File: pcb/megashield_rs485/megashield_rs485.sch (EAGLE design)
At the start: 16 parts, among them J11 DYNAMIXEL_RS485, U1 SN75176B

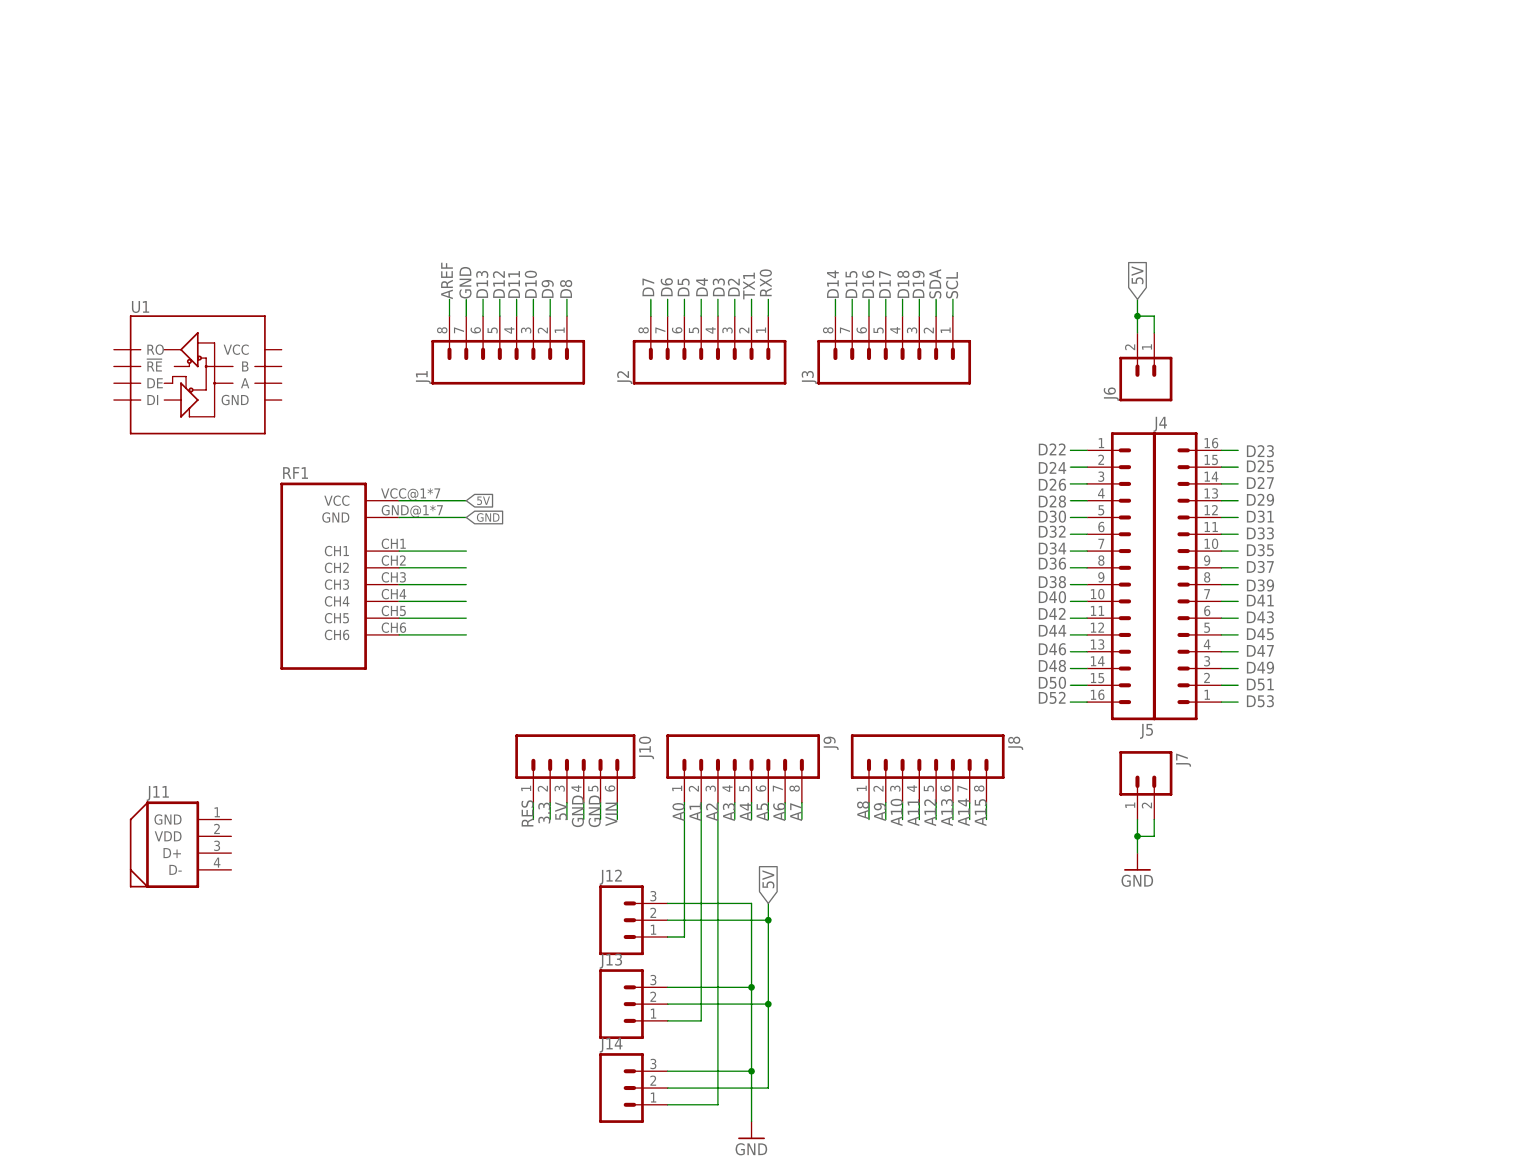
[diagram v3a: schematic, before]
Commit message: PCB con elementos para conexion de pantalla
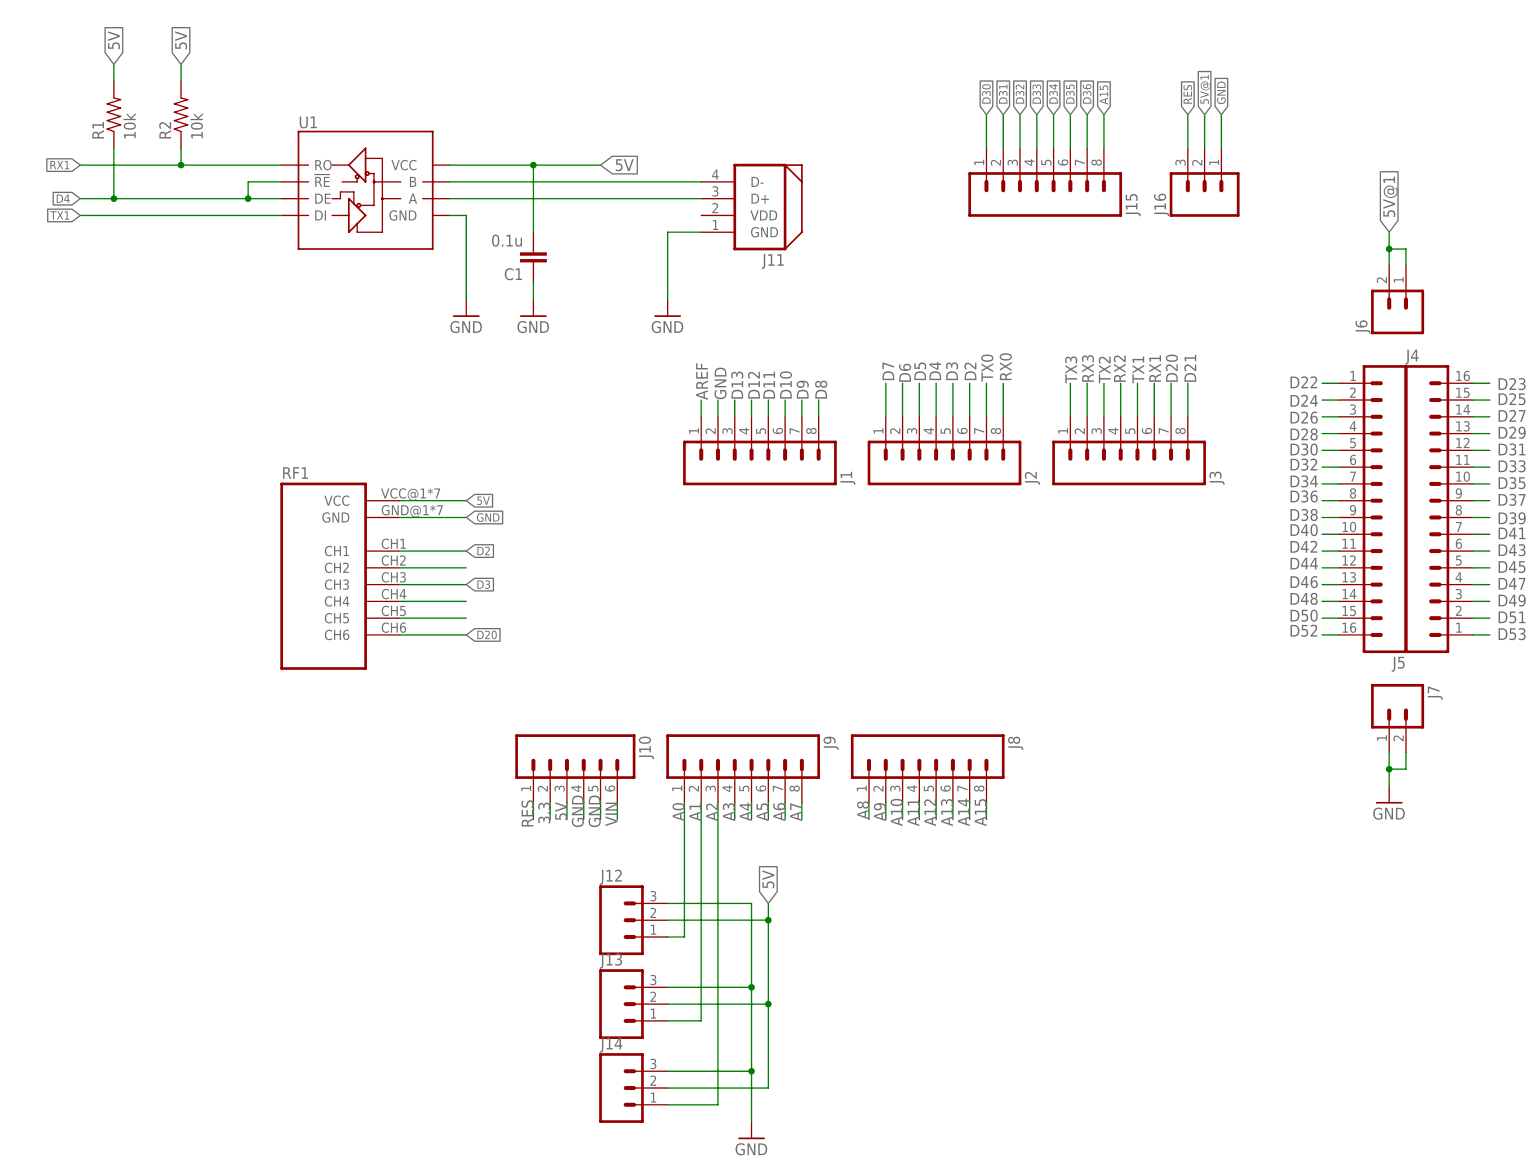
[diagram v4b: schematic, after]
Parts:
- added C1: 0.1u, mecatronica_eagle_lib:CAPPTH
- added J15: (no value), mecatronica_eagle_lib:M08LONGPADS
- added J16: (no value), mecatronica_eagle_lib:M03LONGPADS
- added R1, R2: 10k, mecatronica_eagle_lib:RESISTORPTH-1/4W
- U1: value SN75176B -> RS485
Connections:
- net D14 renamed D21
- net D18 renamed RX2
- net D19 renamed TX2
- net SCL renamed TX3
- net SDA renamed RX3
- removed net D15: J3.7
- removed net D16: J3.6
- removed net D17: J3.5
- removed net N$3: RF1.CH1
- removed net N$5: RF1.CH3
- removed net N$8: RF1.CH6
- new net 5V@1: J16.2, J6.1, J6.2
- new net D20: J3.7, RF1.CH6
- new net N$1: J11.D+, U1.A
- new net N$2: J11.D-, U1.B
- new net RX1: J3.6, R2.1, U1.RO
- new net TX0: J2.7
- net 5V: now also C1.2, R1.2, R2.2, U1.VCC; no longer J6.1, J6.2
- net A15: now also J15.8
- net AREF: now also J1.1; no longer J1.8
- net D10: now also J1.6; no longer J1.3
- net D11: now also J1.5; no longer J1.4
- net D12: now also J1.4; no longer J1.5
- net D13: now also J1.3; no longer J1.6
- net D2: now also J2.6, RF1.CH1; no longer J2.3
- net D3: now also J2.5, RF1.CH3; no longer J2.4
- net D30: now also J15.1
- net D31: now also J15.2
- net D32: now also J15.3
- net D33: now also J15.4
- net D34: now also J15.5
- net D35: now also J15.6
- net D36: now also J15.7
- net D4: now also J2.4, R1.1, U1.!RE, U1.DE; no longer J2.5
- net D5: now also J2.3; no longer J2.6
- net D6: now also J2.2; no longer J2.7
- net D7: now also J2.1; no longer J2.8
- net D8: now also J1.8; no longer J1.1
- net D9: now also J1.7; no longer J1.2
- net GND: now also C1.1, J1.2, J11.GND, J16.1, U1.GND; no longer J1.7
- net RES: now also J16.3
- net RX0: now also J2.8; no longer J2.1
- net TX1: now also J3.5, U1.DI; no longer J2.2
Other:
- moved on the sheet: J1, J11, J2, J3, J4, J5, J6, J7, U1

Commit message: PCB with LCD
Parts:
- removed J15: (no value), mecatronica_eagle_lib:M08LONGPADS
- removed J16: (no value), mecatronica_eagle_lib:M03LONGPADS
- added LCD: LCD_SHIELD, mecatronica_eagle_lib:LCD_SHIELD
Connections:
- net 5V@1: now also LCD.VCC; no longer J16.2
- net A15: now also LCD.BS; no longer J15.8
- net D30: now also LCD.DB4; no longer J15.1
- net D31: now also LCD.DB5; no longer J15.2
- net D32: now also LCD.DB6; no longer J15.3
- net D33: now also LCD.DB7; no longer J15.4
- net D34: now also LCD.RS; no longer J15.5
- net D35: now also LCD.EN; no longer J15.6
- net D36: now also LCD.BLC; no longer J15.7
- net GND: now also LCD.GND; no longer J16.1
- net RES: no longer J16.3
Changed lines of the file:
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@@
 <?xml version="1.0" encoding="utf-8"?>
 <!DOCTYPE eagle SYSTEM "eagle.dtd">
-<eagle version="7.4.0">
+<eagle version="7.6.0">
 <drawing>
 <settings>
@@
 <setting verticaltext="up"/>
 </settings>
-<grid distance="0.1" unitdist="inch" unit="inch" style="lines" multiple="1" display="yes" altdistance="0.01" altunitdist="inch" altunit="inch"/>
+<grid distance="0.1" unitdist="inch" unit="inch" style="lines" multiple="1" display="no" altdistance="0.01" altunitdist="inch" altunit="inch"/>
 <layers>
 <layer number="1" name="Top" color="4" fill="1" visible="no" active="no"/>
@@
 <layer number="230" name="230bmp" color="7" fill="1" visible="yes" active="yes"/>
 <layer number="231" name="231bmp" color="7" fill="1" visible="yes" active="yes"/>
+<layer number="232" name="Eagle3D_PG2" color="7" fill="1" visible="no" active="no"/>
+<layer number="233" name="Eagle3D_PG3" color="7" fill="1" visible="no" active="no"/>
 <layer number="248" name="Housing" color="7" fill="1" visible="yes" active="yes"/>
 <layer number="249" name="Edge" color="7" fill="1" visible="yes" active="yes"/>
@@
 <part name="R2" library="mecatronica_eagle_lib" deviceset="RESISTOR" device="PTH-1/4W" value="10k"/>
 <part name="GND5" library="SparkFun" deviceset="GND" device=""/>
-<part name="J15" library="mecatronica_eagle_lib" deviceset="M08" device="LONGPADS"/>
-<part name="J16" library="mecatronica_eagle_lib" deviceset="M03" device="LONGPADS"/>
+<part name="LCD" library="mecatronica_eagle_lib" deviceset="LCD_SHIELD" device=""/>
 </parts>
 <sheets>
@@
 <instance part="R2" gate="G$1" x="30.48" y="165.1" rot="R90"/>
 <instance part="GND5" gate="1" x="104.14" y="134.62"/>
-<instance part="J15" gate="G$1" x="160.02" y="154.94" rot="MR90"/>
-<instance part="J16" gate="J$1" x="185.42" y="152.4" rot="R90"/>
+<instance part="LCD" gate="G$1" x="154.94" y="157.48"/>
 </instances>
 <busses>
@@
 <label x="83.82" y="57.15" size="1.778" layer="95" rot="R90"/>
 <pinref part="J10" gate="G$1" pin="1"/>
-</segment>
-<segment>
-<pinref part="J16" gate="J$1" pin="3"/>
-<wire x1="182.88" y1="160.02" x2="182.88" y2="165.1" width="0.1524" layer="91"/>
-<label x="182.88" y="165.1" size="1.27" layer="95" rot="R90" xref="yes"/>
 </segment>
 </net>
@@
 </segment>
 <segment>
-<pinref part="J15" gate="G$1" pin="8"/>
-<wire x1="170.18" y1="160.02" x2="170.18" y2="165.1" width="0.1524" layer="91"/>
-<label x="170.18" y="165.1" size="1.27" layer="95" rot="R90" xref="yes"/>
+<wire x1="167.64" y1="142.24" x2="175.26" y2="142.24" width="0.1524" layer="91"/>
+<label x="175.26" y="142.24" size="1.27" layer="95" xref="yes"/>
+<pinref part="LCD" gate="G$1" pin="BS"/>
 </segment>
 </net>
@@
 </segment>
 <segment>
-<pinref part="J15" gate="G$1" pin="1"/>
-<wire x1="152.4" y1="160.02" x2="152.4" y2="165.1" width="0.1524" layer="91"/>
-<label x="152.4" y="165.1" size="1.27" layer="95" rot="R90" xref="yes"/>
+<wire x1="167.64" y1="162.56" x2="175.26" y2="162.56" width="0.1524" layer="91"/>
+<label x="175.26" y="162.56" size="1.27" layer="95" xref="yes"/>
+<pinref part="LCD" gate="G$1" pin="DB4"/>
 </segment>
 </net>
@@
 </segment>
 <segment>
-<pinref part="J15" gate="G$1" pin="3"/>
-<wire x1="157.48" y1="160.02" x2="157.48" y2="165.1" width="0.1524" layer="91"/>
-<label x="157.48" y="165.1" size="1.27" layer="95" rot="R90" xref="yes"/>
+<wire x1="167.64" y1="157.48" x2="175.26" y2="157.48" width="0.1524" layer="91"/>
+<label x="175.26" y="157.48" size="1.27" layer="95" xref="yes"/>
+<pinref part="LCD" gate="G$1" pin="DB6"/>
 </segment>
 </net>
@@
 </segment>
 <segment>
-<pinref part="J15" gate="G$1" pin="5"/>
-<wire x1="162.56" y1="160.02" x2="162.56" y2="165.1" width="0.1524" layer="91"/>
-<label x="162.56" y="165.1" size="1.27" layer="95" rot="R90" xref="yes"/>
+<wire x1="167.64" y1="147.32" x2="175.26" y2="147.32" width="0.1524" layer="91"/>
+<label x="175.26" y="147.32" size="1.27" layer="95" xref="yes"/>
+<pinref part="LCD" gate="G$1" pin="RS"/>
 </segment>
 </net>
@@
 </segment>
 <segment>
-<pinref part="J15" gate="G$1" pin="7"/>
-<wire x1="167.64" y1="160.02" x2="167.64" y2="165.1" width="0.1524" layer="91"/>
-<label x="167.64" y="165.1" size="1.27" layer="95" rot="R90" xref="yes"/>
+<wire x1="167.64" y1="144.78" x2="175.26" y2="144.78" width="0.1524" layer="91"/>
+<label x="175.26" y="144.78" size="1.27" layer="95" xref="yes"/>
+<pinref part="LCD" gate="G$1" pin="BLC"/>
 </segment>
 </net>
@@
 </segment>
 <segment>
-<pinref part="J15" gate="G$1" pin="2"/>
-<wire x1="154.94" y1="160.02" x2="154.94" y2="165.1" width="0.1524" layer="91"/>
-<label x="154.94" y="165.1" size="1.27" layer="95" rot="R90" xref="yes"/>
+<wire x1="167.64" y1="160.02" x2="175.26" y2="160.02" width="0.1524" layer="91"/>
+<label x="175.26" y="160.02" size="1.27" layer="95" xref="yes"/>
+<pinref part="LCD" gate="G$1" pin="DB5"/>
 </segment>
 </net>
@@
 </segment>
 <segment>
-<pinref part="J15" gate="G$1" pin="4"/>
-<wire x1="160.02" y1="160.02" x2="160.02" y2="165.1" width="0.1524" layer="91"/>
-<label x="160.02" y="165.1" size="1.27" layer="95" rot="R90" xref="yes"/>
+<wire x1="167.64" y1="154.94" x2="175.26" y2="154.94" width="0.1524" layer="91"/>
+<label x="175.26" y="154.94" size="1.27" layer="95" xref="yes"/>
+<pinref part="LCD" gate="G$1" pin="DB7"/>
 </segment>
 </net>
@@
 </segment>
 <segment>
-<pinref part="J15" gate="G$1" pin="6"/>
-<wire x1="165.1" y1="160.02" x2="165.1" y2="165.1" width="0.1524" layer="91"/>
-<label x="165.1" y="165.1" size="1.27" layer="95" rot="R90" xref="yes"/>
+<wire x1="167.64" y1="149.86" x2="175.26" y2="149.86" width="0.1524" layer="91"/>
+<label x="175.26" y="149.86" size="1.27" layer="95" xref="yes"/>
+<pinref part="LCD" gate="G$1" pin="EN"/>
 </segment>
 </net>
@@
 </segment>
 <segment>
-<pinref part="J16" gate="J$1" pin="1"/>
-<wire x1="187.96" y1="160.02" x2="187.96" y2="165.1" width="0.1524" layer="91"/>
-<label x="187.96" y="165.1" size="1.27" layer="95" rot="R90" xref="yes"/>
+<wire x1="167.64" y1="167.64" x2="175.26" y2="167.64" width="0.1524" layer="91"/>
+<label x="175.26" y="167.64" size="1.27" layer="95" xref="yes"/>
+<pinref part="LCD" gate="G$1" pin="GND"/>
 </segment>
 </net>
@@
 </segment>
 <segment>
-<pinref part="J16" gate="J$1" pin="2"/>
-<wire x1="185.42" y1="160.02" x2="185.42" y2="165.1" width="0.1524" layer="91"/>
-<label x="185.42" y="165.1" size="1.27" layer="95" rot="R90" xref="yes"/>
-</segment>
-</net>
+<wire x1="167.64" y1="170.18" x2="175.26" y2="170.18" width="0.1524" layer="91"/>
+<label x="175.26" y="170.18" size="1.27" layer="95" xref="yes"/>
+<pinref part="LCD" gate="G$1" pin="VCC"/>
+</segment>
+</net>
